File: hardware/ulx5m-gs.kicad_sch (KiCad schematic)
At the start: 4 parts

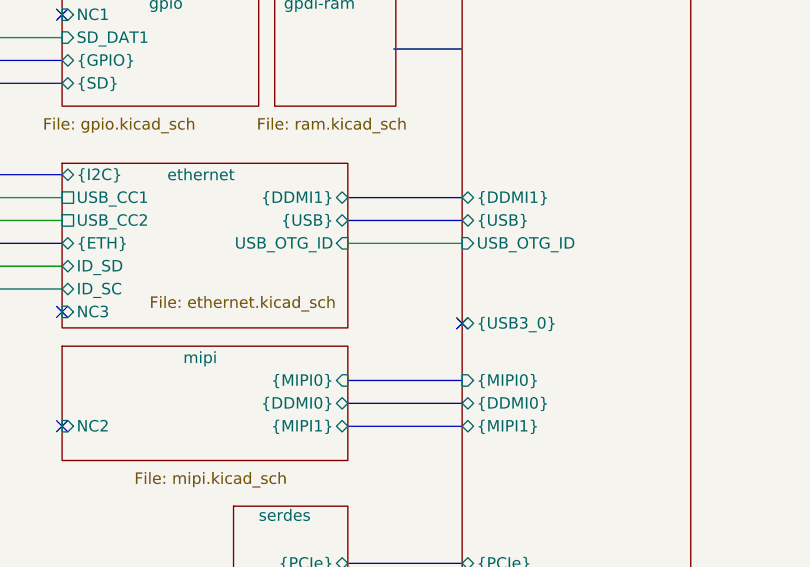
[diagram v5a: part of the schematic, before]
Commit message: Clearing all ERC, rounting diff
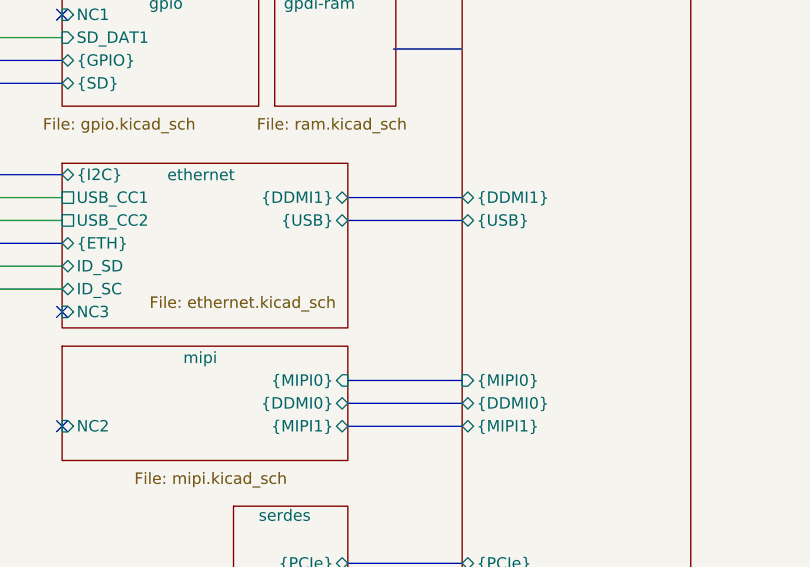
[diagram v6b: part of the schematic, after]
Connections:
- no-connect marks 17 -> 16
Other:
- sheet cm4-hsio ports: added none; removed USB_OTG_ID, {USB3_0}
- sheet ethernet ports: added none; removed USB_OTG_ID
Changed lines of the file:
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@@
-	)
-	(no_connect
-		(at 233.68 101.6)
 	)
 	(no_connect
@@
 		(pts
 			(xy 176.53 97.79) (xy 189.23 97.79)
-		)
-		(stroke
-			(width 0)
-			(type default)
-		)
-	)
-	(wire
-		(pts
-			(xy 220.98 92.71) (xy 233.68 92.71)
 		)
 		(stroke
@@
 			)
 		)
-		(pin "USB_OTG_ID" input
-			(at 220.98 92.71 0)
-			(effects
-				(font
-					(size 1.27 1.27)
-				)
-				(justify right)
-			)
-		)
 		(instances
 			(project "ulx5m-gs"
@@
 			)
 		)
-		(pin "{USB3_0}" bidirectional
-			(at 233.68 101.6 180)
-			(effects
-				(font
-					(size 1.27 1.27)
-				)
-				(justify left)
-			)
-		)
 		(pin "{MIPI1}" bidirectional
 			(at 233.68 113.03 180)
 			(effects
 				(font
-					(size 1.27 1.27)
-				)
-				(justify left)
-			)
-		)
-		(pin "USB_OTG_ID" input
-			(at 233.68 92.71 180)
-			(effects
-				(font

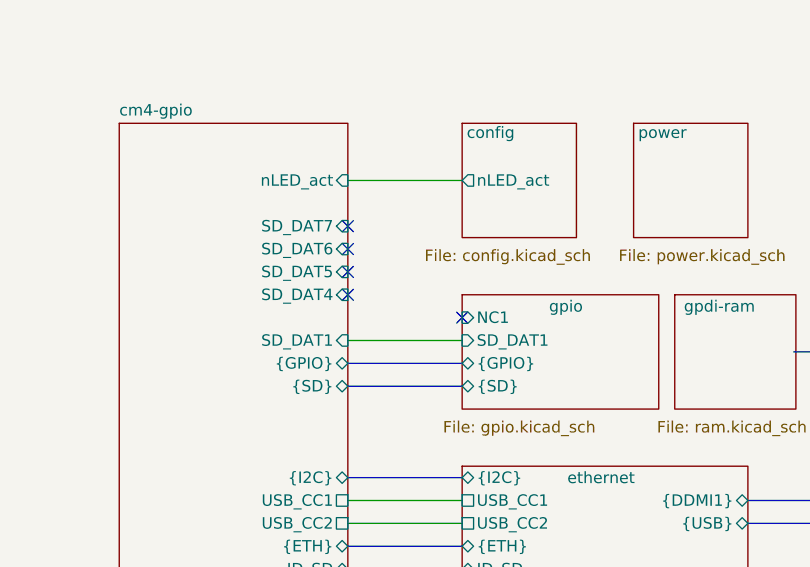
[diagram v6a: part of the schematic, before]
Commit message: Routing BTNs, LEDs, CLK
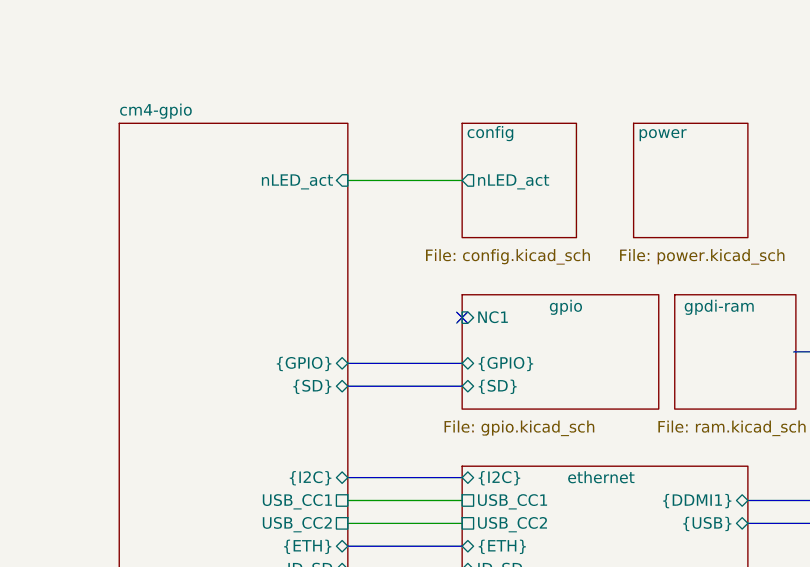
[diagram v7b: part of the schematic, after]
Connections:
- no-connect marks 16 -> 12
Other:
- sheet cm4-gpio ports: added none; removed SD_DAT1, SD_DAT4, SD_DAT5, SD_DAT6, SD_DAT7
- sheet gpio ports: added none; removed SD_DAT1
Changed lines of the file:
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@@
-	)
-	(no_connect
-		(at 176.53 57.15)
 	)
 	(no_connect
@@
 	)
 	(no_connect
-		(at 176.53 64.77)
-	)
-	(no_connect
 		(at 176.53 114.3)
 	)
@@
 	)
 	(no_connect
-		(at 176.53 59.69)
-	)
-	(no_connect
-		(at 176.53 62.23)
-	)
-	(no_connect
 		(at 176.53 129.54)
 	)
@@
 		(pts
 			(xy 176.53 95.25) (xy 189.23 95.25)
-		)
-		(stroke
-			(width 0)
-			(type default)
-		)
-	)
-	(wire
-		(pts
-			(xy 176.53 69.85) (xy 189.23 69.85)
 		)
 		(stroke
@@
 			)
 		)
-		(pin "SD_DAT1" input
-			(at 176.53 69.85 0)
-			(effects
-				(font
-					(size 1.27 1.27)
-				)
-				(justify right)
-			)
-		)
-		(pin "SD_DAT4" input
-			(at 176.53 64.77 0)
-			(effects
-				(font
-					(size 1.27 1.27)
-				)
-				(justify right)
-			)
-		)
-		(pin "SD_DAT5" input
-			(at 176.53 62.23 0)
-			(effects
-				(font
-					(size 1.27 1.27)
-				)
-				(justify right)
-			)
-		)
-		(pin "SD_DAT6" input
-			(at 176.53 59.69 0)
-			(effects
-				(font
-					(size 1.27 1.27)
-				)
-				(justify right)
-			)
-		)
-		(pin "SD_DAT7" input
-			(at 176.53 57.15 0)
-			(effects
-				(font
-					(size 1.27 1.27)
-				)
-				(justify right)
-			)
-		)
 		(instances
 			(project "ulx5m-gs"
@@
 			(effects
 				(font
-					(size 1.27 1.27)
-				)
-				(justify left)
-			)
-		)
-		(pin "SD_DAT1" input
-			(at 189.23 69.85 180)
-			(effects
-				(font

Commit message: Cleanup
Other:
- moved on the sheet: H1, H2, H3, H4
